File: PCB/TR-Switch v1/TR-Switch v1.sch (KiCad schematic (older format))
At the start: 24 parts

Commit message: - schematic almost finished - added SPICE (TINA-TI) simulation
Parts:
- removed Q?: Q_NPN_BCE, symbol Device:Q_NPN_BCE
- removed Q?: Q_PNP_BCE, symbol Device:Q_PNP_BCE
- removed R? (x2): R, symbol Device:R
- added C? (x4): C, symbol Device:C
- added C?: 10uF, symbol Device:C
- added J?: Tx Gate, symbol Connector_Generic:Conn_01x02
- added J?: 13V Power In, symbol Connector_Generic:Conn_01x02
- added R? (x5): R, symbol Device:R
- added R? (x3): 100, symbol Device:R
- added R? (x2): 1, symbol Device:R
- added U?: LM317_3PinPackage, symbol Regulator_Linear:LM317_3PinPackage
- added U?: OPA551U, Package_SO:SOIC-8_3.9x4.9mm_P1.27mm, symbol Amplifier_Operational:OPA551U
- added U?: L78L12_TO92, Package_TO_SOT_THT:TO-92_Inline, symbol Regulator_Linear:L78L12_TO92
- added U?: LM337_TO220, Package_TO_SOT_THT:TO-220-3_Vertical, symbol Regulator_Linear:LM337_TO220
- added U? (x2): LM285Z-2.5, Package_TO_SOT_THT:TO-92_Inline, symbol Reference_Voltage:LM285Z-2.5
- added U?: SCLF-X-21.4+, RF_Mini-Circuits:Mini-Circuits_GP731_LandPatternPL-176, symbol RF_Filter:SCLF-X
- C?: value C -> 0.1nF
- C? (x4): value C -> 0.1uF
- C? (x2): value C -> 187pF
- J?: value Conn_Coaxial -> TX
- J?: value Conn_Coaxial -> Coil
- J?: value Conn_Coaxial -> RX
- L?: value L -> 468nH
- L? (x2): value L -> 70nH
- L?: value L -> 2.2uH
- R? (x2): value R -> 91
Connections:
- net labels added: +6V, GNDREF
- wire segments 33 -> 98
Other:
- note added: "Values are for 17MHz"

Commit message: finished v1.0 pcb
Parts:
- removed C?: 0.1nF, symbol Device:C
- removed D? (x2): DIODE, symbol EtherDue-rescue:DIODE
- removed U?: L78L12_TO92, Package_TO_SOT_THT:TO-92_Inline, symbol Regulator_Linear:L78L12_TO92
- removed U? (x2): LM285Z-2.5, Package_TO_SOT_THT:TO-92_Inline, symbol Reference_Voltage:LM285Z-2.5
- added C10, C11, C14, C15: x, Capacitor_SMD:C_0805_2012Metric_Pad1.15x1.40mm_HandSolder, symbol Device:C
- added C19: 0.1nF, Capacitor_SMD:C_0805_2012Metric_Pad1.15x1.40mm_HandSolder, symbol Device:C
- added C2, C5, C6: 1nF, Capacitor_SMD:C_0805_2012Metric_Pad1.15x1.40mm_HandSolder, symbol Device:C
- added C20: 1uF, Capacitor_SMD:C_0805_2012Metric_Pad1.15x1.40mm_HandSolder, symbol Device:C
- added D1, D3: 2.5V Z-Diode, Diode_SMD:D_MiniMELF, symbol Device:D_Zener
- added D2, D4: MA4P7001F, PIN Diodes:D_MELF_1072, symbol Device:D
- added D5: PWR 6V, LED_SMD:LED_1206_3216Metric_Pad1.42x1.75mm_HandSolder, symbol Device:LED
- added R16: 220, Resistor_SMD:R_0805_2012Metric_Pad1.15x1.40mm_HandSolder, symbol Device:R
- added R17, R19: 68.1 0.75W, Resistor_SMD:R_2010_5025Metric_Pad1.52x2.65mm_HandSolder, symbol Device:R
- added R2, R3, R6: 10K, Resistor_SMD:R_0805_2012Metric_Pad1.15x1.40mm_HandSolder, symbol Device:R
- added R7, R8: 1K, Resistor_SMD:R_0805_2012Metric_Pad1.15x1.40mm_HandSolder, symbol Device:R
- added U1: L7812, Package_TO_SOT_THT:TO-220-3_Vertical, symbol Regulator_Linear:L7812
- C1, C12, C13, C17, C18, C3, C9: renamed from C?; footprint (none) -> Capacitor_SMD:C_0805_2012Metric_Pad1.15x1.40mm_HandSolder
- C16, C7, C8: renamed from C?; value C -> 1uF; footprint (none) -> Capacitor_SMD:C_0805_2012Metric_Pad1.15x1.40mm_HandSolder
- C4: renamed from C?; value C -> 10uF; footprint (none) -> Capacitor_SMD:C_0805_2012Metric_Pad1.15x1.40mm_HandSolder
- J1, J2: renamed from J?; footprint (none) -> Connector_PinHeader_2.54mm:PinHeader_1x02_P2.54mm_Vertical
- J3, J4, J5: renamed from J?; footprint (none) -> Connector_Coaxial:SMA_Amphenol_132134_Vertical
- L1, L3, L4: renamed from L?; footprint (none) -> Inductances:Wuerth_Fixed_Inductors_WE-GFH
- L2: renamed from L?; footprint (none) -> Inductances:L_Axial_L20.0mm_D8.0mm_P25.40mm_Horizontal
- R1, R12, R13, R14, R15: renamed from R?; footprint (none) -> Resistor_SMD:R_0805_2012Metric_Pad1.15x1.40mm_HandSolder
- R10, R4, R5, R9: renamed from R?; value R -> 10K; footprint (none) -> Resistor_SMD:R_0805_2012Metric_Pad1.15x1.40mm_HandSolder
- R11: renamed from R?; value R -> 1; footprint (none) -> Resistor_SMD:R_0805_2012Metric_Pad1.15x1.40mm_HandSolder
- R18, R20: renamed from R?; value 91 -> 22.1 0.25W; footprint (none) -> Resistor_SMD:R_0603_1608Metric_Pad1.05x0.95mm_HandSolder
- U3: renamed from U?; value LM317_3PinPackage -> LM317_TO220; footprint (none) -> Package_TO_SOT_THT:TO-220-3_Vertical
- U7: renamed from U?; footprint RF_Mini-Circuits:Mini-Circuits_GP731_LandPatternPL-176 -> RF_Mini-Circuits:Mini-Circuits_YY161_LandPatternPL-049
- gave numbers to parts that had none: 4
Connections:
- net +12V: now also C20.1, U1.3 (OUT)
- net +6V: now also D4.1 (K), D5.2 (A)
- net GND: now also C10.2, C11.2, C14.2, C15.2, C20.2, D1.2 (A), R16.2, U1.2 (GND)
- net at C3.1, L1.2: now also D2.2 (A)
- net at C12.1, C9.1, L2.1: now also C10.1, C11.1, D2.1 (K)
- net at R13.1, U3.1 (ADJ): now also D3.2 (A)
- net at C13.1, C17.2, L2.2: now also C14.1, C15.1, D4.2 (A)
- net at J5.1 (In): now also U7.8 (OUT)
- net at J1.2 (Pin_2): now also R3.1; no longer R5.1
- net at R4.2, R9.1, U2.2 (-): now also R6.2, R7.1
- net at R10.1, R5.2, U2.3 (+): now also R6.1, R8.1
- net at R11.1, R9.2, U2.6: now also C5.1
- net at L4.2, U6.3: now also C19.2; no longer U7.1 (IN)
- net at L1.1, R10.2, R11.2: now also C6.1
- net at R4.1: now also C2.1, R2.2; no longer R1.2
- net at L3.1: now also R17.2; no longer R18.2
- net at L4.1: now also R19.2; no longer R20.2
- net at C1.1, J2.2 (Pin_2): now also U1.1 (IN)
- net at R12.2, U4.1 (ADJ): now also D3.1 (K)
- new net: C5.2, R7.2
- new net: C2.2, R3.2, R5.1
- new net: R17.1, R18.2
- new net: R19.1, R20.2
- new net: C6.2, R8.2
- new net: D1.1 (K), R1.2, R2.1
- new net: D5.1 (K), R16.1
- new net: C19.1, U7.1 (IN)
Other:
- moved on the sheet: C12, C13, C17, C18, C3, C9, J1, J3, J4, J5, L1, L2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

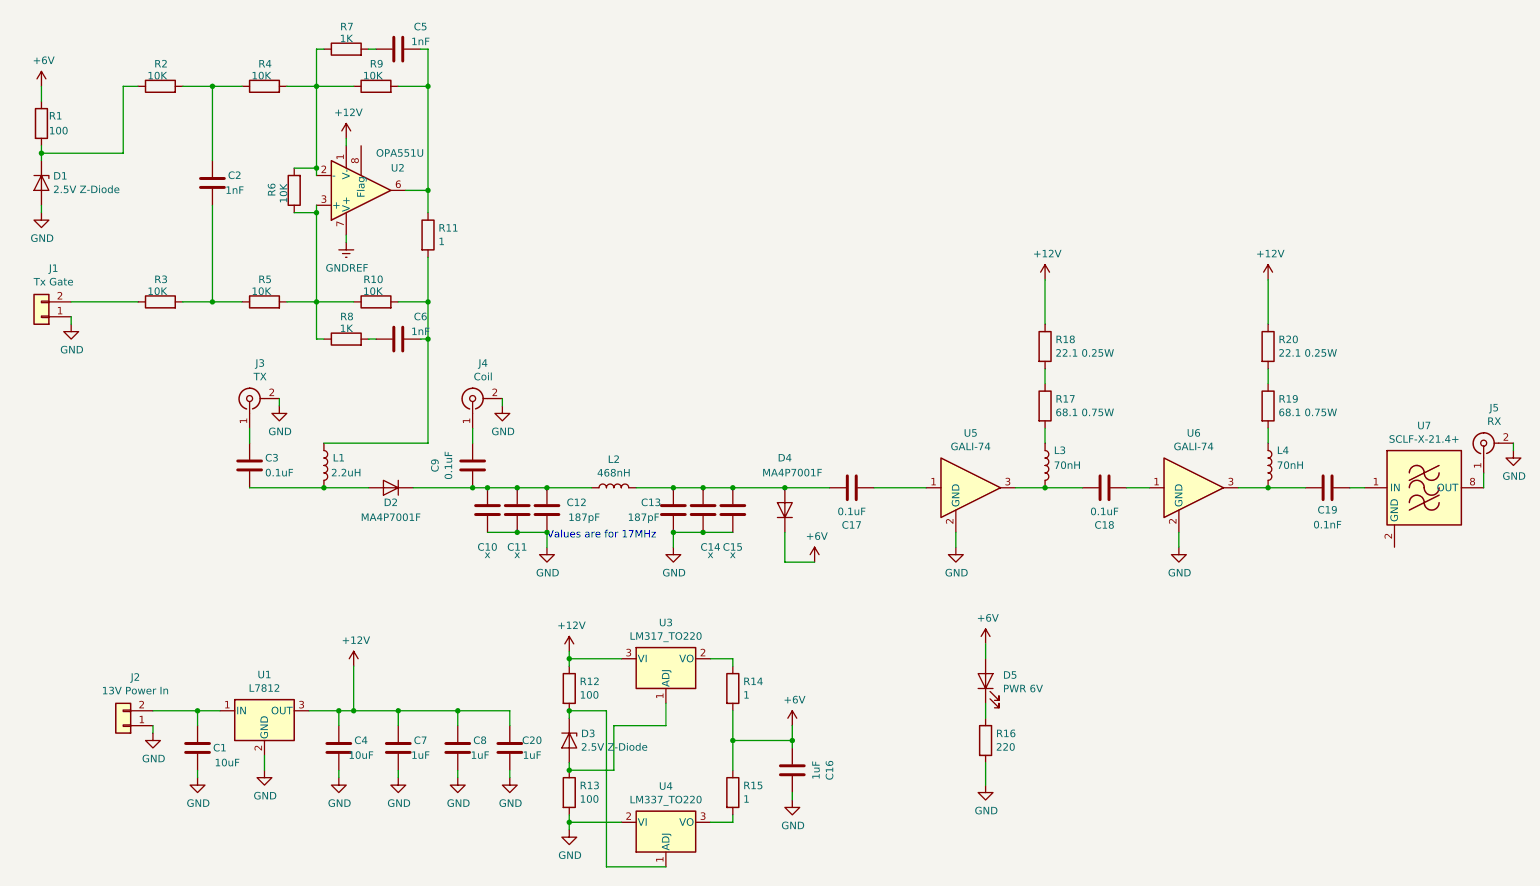
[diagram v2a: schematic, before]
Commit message: - Fehler behoben - Kondensatoren hinzugefügt
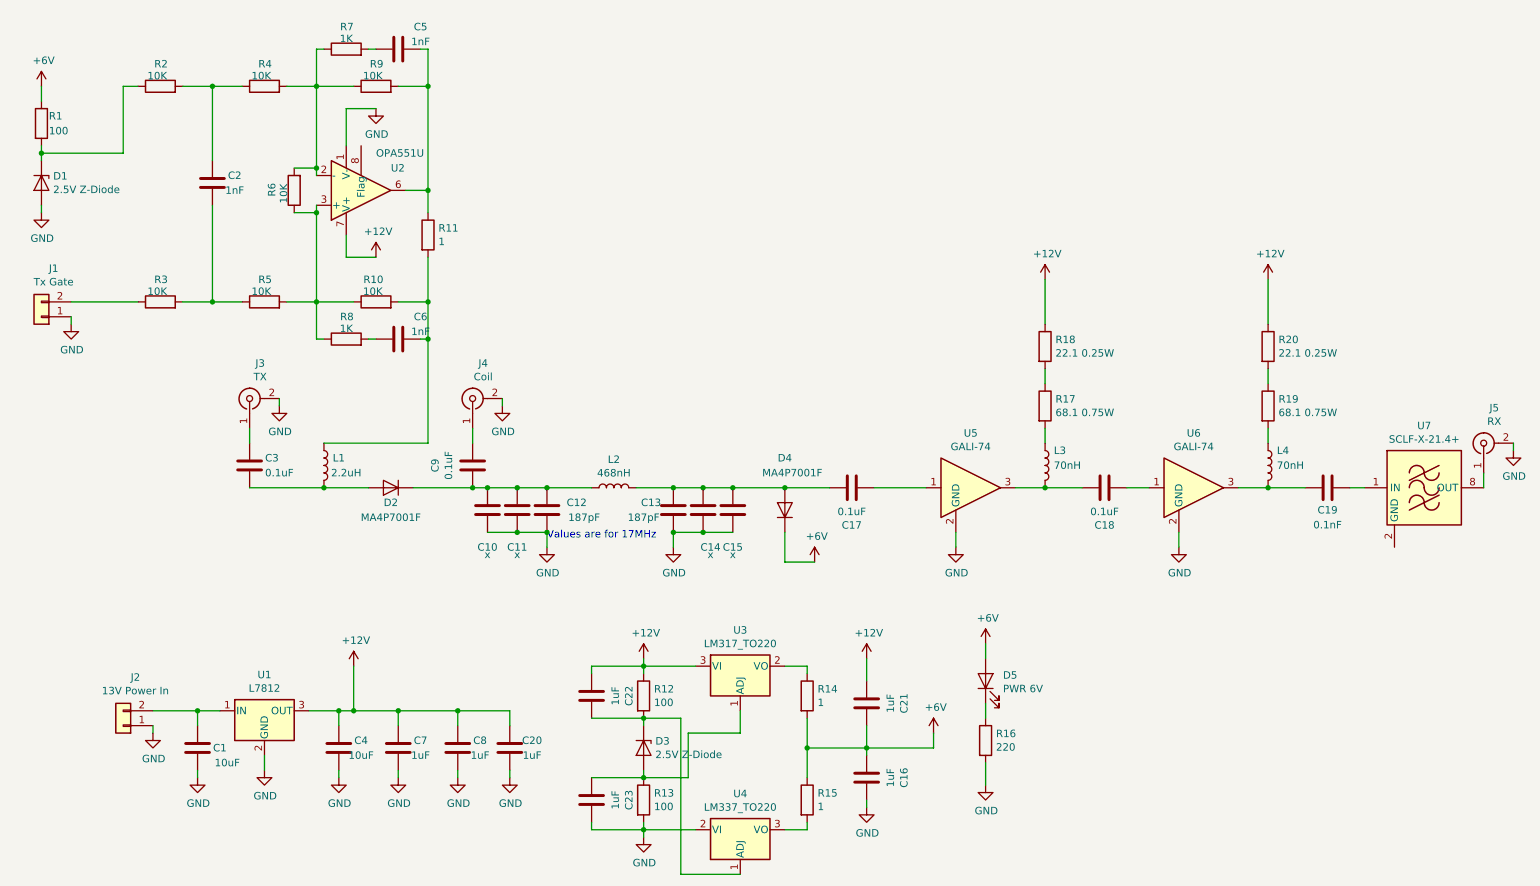
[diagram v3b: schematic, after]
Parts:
- added C21, C22, C23: 1uF, Capacitor_SMD:C_0805_2012Metric_Pad1.15x1.40mm_HandSolder, symbol Device:C
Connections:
- net GNDREF is gone; now on net +12V: U2.7 (V+)
- net +12V: now also C21.1, C22.1; no longer U2.1 (V-), U2.4 (V-), U2.5 (V-)
- net +6V: now also C21.2
- net GND: now also U2.1 (V-), U2.4 (V-), U2.5 (V-), C23.2
- net at D3.2 (A), R13.1, U3.1 (ADJ): now also C23.1
- net at D3.1 (K), R12.2, U4.1 (ADJ): now also C22.2
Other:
- moved on the sheet: C16, D3, R12, R13, R14, R15, U3, U4

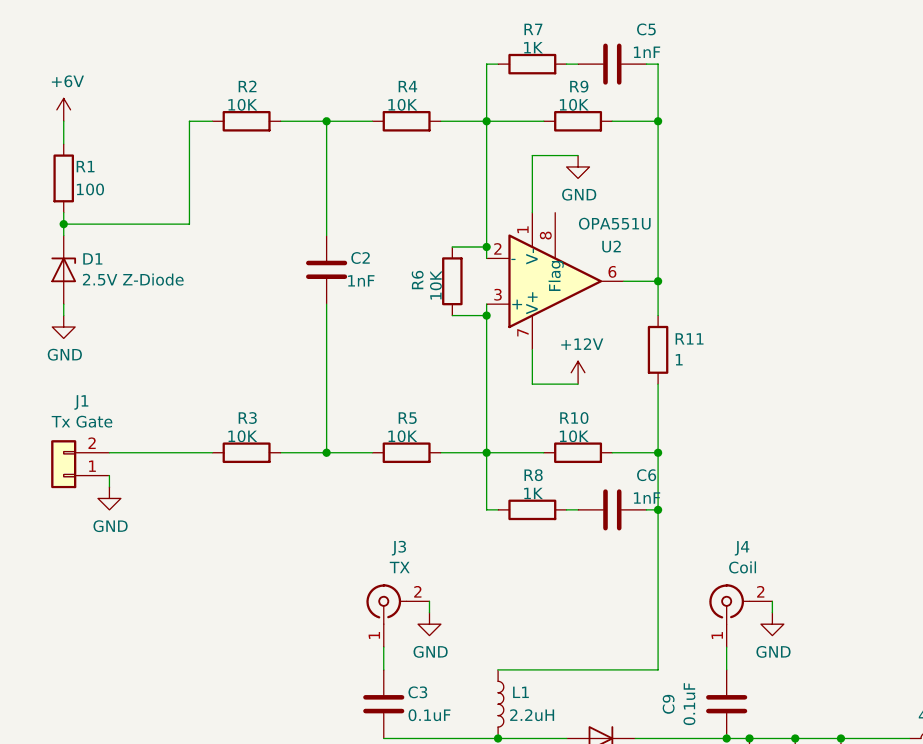
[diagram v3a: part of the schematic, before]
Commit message: updated component values and simulation rise / falltime is about 3 us
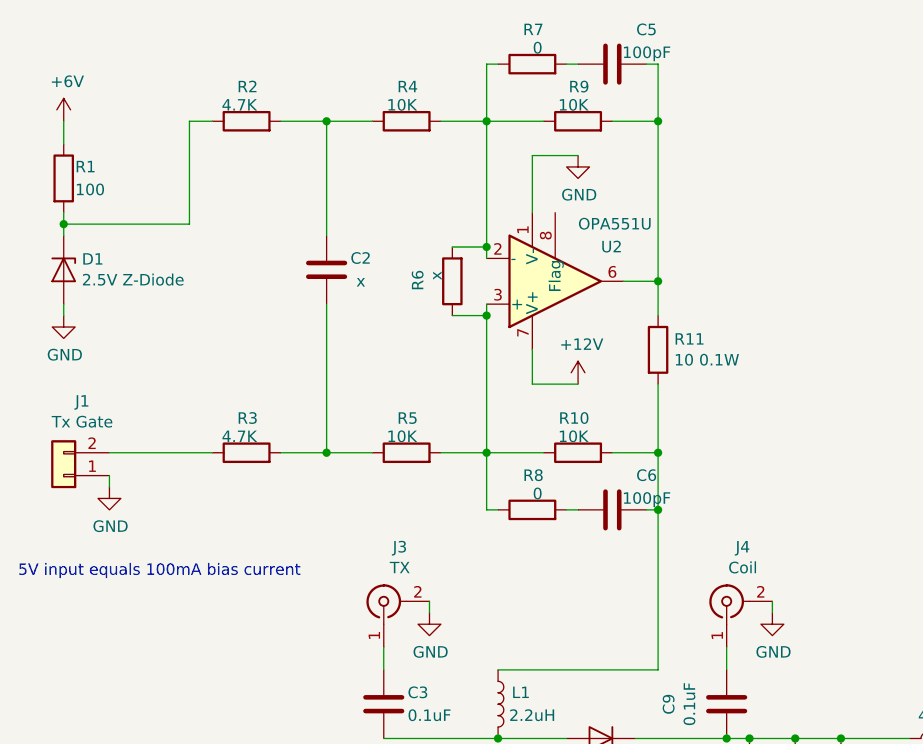
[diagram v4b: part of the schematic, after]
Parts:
- C2: value 1nF -> x
- C5, C6: value 1nF -> 100pF
- R11: value 1 -> 10 0.1W
- R2, R3: value 10K -> 4.7K
- R6: value 10K -> x
- R7, R8: value 1K -> 0
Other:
- note added: "5V input equals 100mA bias current"
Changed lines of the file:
@@
 P 3750 2200
 F 0 "R11" H 3820 2246 50  0000 L CNN
-F 1 "1" H 3820 2155 50  0000 L CNN
+F 1 "10 0.1W" H 3820 2155 50  0000 L CNN
 F 2 "Resistor_SMD:R_0805_2012Metric_Pad1.15x1.40mm_HandSolder" V 3680 2200 50  0001 C CNN
 F 3 "~" H 3750 2200 50  0001 C CNN
@@
 P 3200 950
 F 0 "R7" V 3350 900 50  0000 L CNN
-F 1 "1K" V 3270 905 50  0000 L CNN
+F 1 "0" V 3270 905 50  0000 L CNN
 F 2 "Resistor_SMD:R_0805_2012Metric_Pad1.15x1.40mm_HandSolder" V 3130 950 50  0001 C CNN
 F 3 "~" H 3200 950 50  0001 C CNN
@@
 P 3550 950
 F 0 "C5" V 3400 1100 50  0000 C CNN
-F 1 "1nF" V 3500 1100 50  0000 C CNN
+F 1 "100pF" V 3500 1100 50  0000 C CNN
 F 2 "Capacitor_SMD:C_0805_2012Metric_Pad1.15x1.40mm_HandSolder" H 3588 800 50  0001 C CNN
 F 3 "~" H 3550 950 50  0001 C CNN
@@
 P 3200 2900
 F 0 "R8" V 3350 2850 50  0000 L CNN
-F 1 "1K" V 3270 2855 50  0000 L CNN
+F 1 "0" V 3270 2855 50  0000 L CNN
 F 2 "Resistor_SMD:R_0805_2012Metric_Pad1.15x1.40mm_HandSolder" V 3130 2900 50  0001 C CNN
 F 3 "~" H 3200 2900 50  0001 C CNN
@@
 P 3550 2900
 F 0 "C6" V 3400 3050 50  0000 C CNN
-F 1 "1nF" V 3500 3050 50  0000 C CNN
+F 1 "100pF" V 3500 3050 50  0000 C CNN
 F 2 "Capacitor_SMD:C_0805_2012Metric_Pad1.15x1.40mm_HandSolder" H 3588 2750 50  0001 C CNN
 F 3 "~" H 3550 2900 50  0001 C CNN
@@
 P 2850 1900
 F 0 "R6" V 3000 1850 50  0000 L CNN
-F 1 "10K" V 2920 1855 50  0000 L CNN
+F 1 "x" V 2920 1855 50  0000 L CNN
 F 2 "Resistor_SMD:R_0805_2012Metric_Pad1.15x1.40mm_HandSolder" V 2780 1900 50  0001 C CNN
 F 3 "~" H 2850 1900 50  0001 C CNN
@@
 P 1950 2650
 F 0 "R3" V 2100 2600 50  0000 L CNN
-F 1 "10K" V 2020 2605 50  0000 L CNN
+F 1 "4.7K" V 2020 2605 50  0000 L CNN
 F 2 "Resistor_SMD:R_0805_2012Metric_Pad1.15x1.40mm_HandSolder" V 1880 2650 50  0001 C CNN
 F 3 "~" H 1950 2650 50  0001 C CNN
@@
 P 1950 1200
 F 0 "R2" V 2100 1150 50  0000 L CNN
-F 1 "10K" V 2020 1155 50  0000 L CNN
+F 1 "4.7K" V 2020 1155 50  0000 L CNN
 F 2 "Resistor_SMD:R_0805_2012Metric_Pad1.15x1.40mm_HandSolder" V 1880 1200 50  0001 C CNN
 F 3 "~" H 1950 1200 50  0001 C CNN
@@
 P 2300 1850
 F 0 "C2" H 2450 1900 50  0000 C CNN
-F 1 "1nF" H 2450 1800 50  0000 C CNN
+F 1 "x" H 2450 1800 50  0000 C CNN
 F 2 "Capacitor_SMD:C_0805_2012Metric_Pad1.15x1.40mm_HandSolder" H 2338 1700 50  0001 C CNN
 F 3 "~" H 2300 1850 50  0001 C CNN
@@
 Wire Wire Line
 	3200 1350 3200 1600
+Text Notes 950  3200 0    50   ~ 0
+5V input equals 100mA bias current
 $EndSCHEMATC

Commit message: updated component value
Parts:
- R2, R3: value 4.7K -> 15k
- U5, U6: symbol RF_Amplifier:GALI-74 -> TR-Switch-v1-rescue:GALI-74-RF_Amplifier
- U7: symbol RF_Filter:SCLF-X -> TR-Switch-v1-rescue:SCLF-X-RF_Filter
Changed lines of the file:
@@
 	5400 4200 5400 4300
 $Comp
-L RF_Amplifier:GALI-74 U5
+L TR-Switch-v1-rescue:GALI-74-RF_Amplifier U5
 U 1 1 5F0C5BD5
 P 7400 3900
@@
 $EndComp
 $Comp
-L RF_Amplifier:GALI-74 U6
+L TR-Switch-v1-rescue:GALI-74-RF_Amplifier U6
 U 1 1 5F0C9C89
 P 8900 3900
@@
 Values are for 17MHz
 $Comp
-L RF_Filter:SCLF-X U7
+L TR-Switch-v1-rescue:SCLF-X-RF_Filter U7
 U 1 1 5F1D807A
 P 10450 3900
@@
 P 1950 2650
 F 0 "R3" V 2100 2600 50  0000 L CNN
-F 1 "4.7K" V 2020 2605 50  0000 L CNN
+F 1 "15k" V 2020 2605 50  0000 L CNN
 F 2 "Resistor_SMD:R_0805_2012Metric_Pad1.15x1.40mm_HandSolder" V 1880 2650 50  0001 C CNN
 F 3 "~" H 1950 2650 50  0001 C CNN
@@
 P 1950 1200
 F 0 "R2" V 2100 1150 50  0000 L CNN
-F 1 "4.7K" V 2020 1155 50  0000 L CNN
+F 1 "15k" V 2020 1155 50  0000 L CNN
 F 2 "Resistor_SMD:R_0805_2012Metric_Pad1.15x1.40mm_HandSolder" V 1880 1200 50  0001 C CNN
 F 3 "~" H 1950 1200 50  0001 C CNN
